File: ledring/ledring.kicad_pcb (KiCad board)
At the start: 2 copper layers, 92 x 92 mm, 22 parts, among them U1 LM3914V, U2 LM3914V

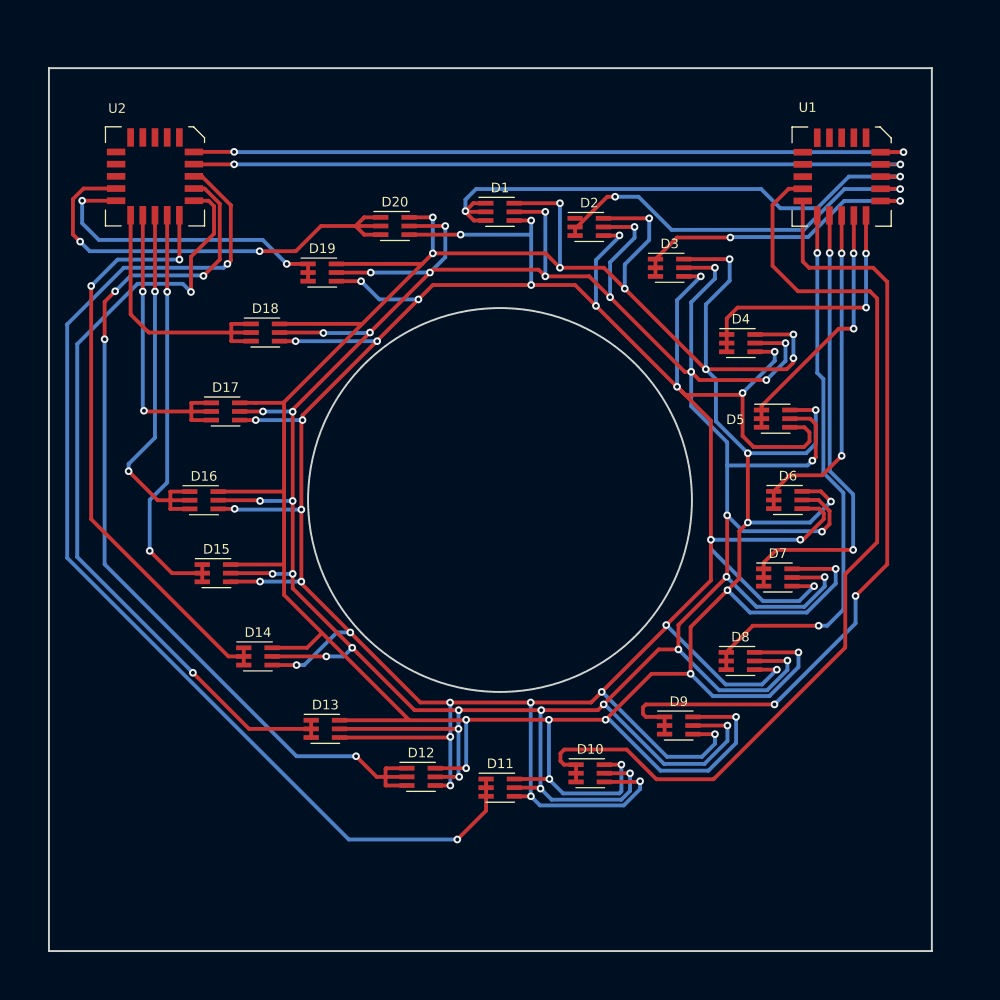
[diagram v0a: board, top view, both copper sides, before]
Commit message: ledring: Adjust PCB routing (angles)
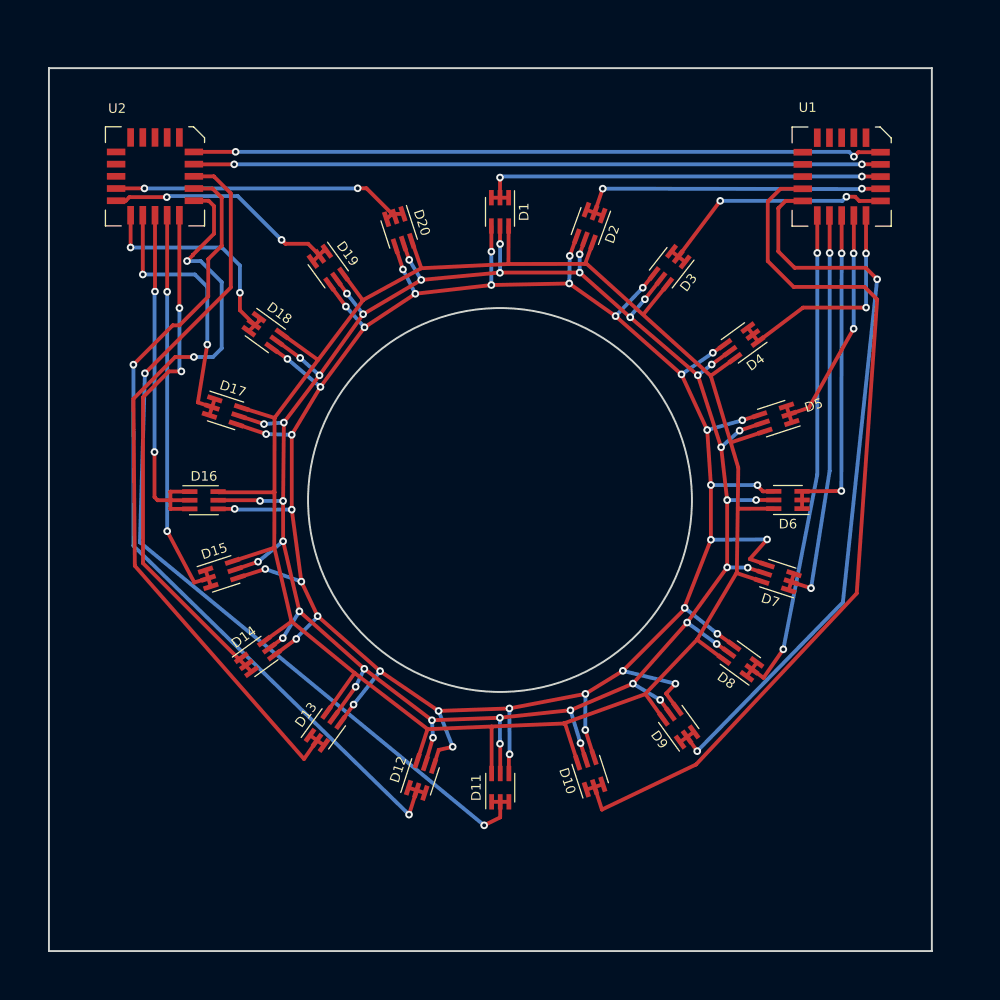
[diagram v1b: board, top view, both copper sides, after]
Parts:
- moved D19 0.80 mm to (112.1, 75.8), turned to -54 degrees
- moved D20 0.61 mm to (119.5, 71.9), turned to -72 degrees
- moved D15 0.56 mm to (101.0, 107.7), turned to 18 degrees
- moved D2 0.11 mm to (139.3, 71.5), turned to -110 degrees
- moved D4 0.06 mm to (155.2, 83.6), turned to -144 degrees
- turned D10 to 108 degrees
- turned D1 to -90 degrees
- turned D11 to 90 degrees
- turned D12 to 72 degrees
- turned D13 to 54 degrees
- turned D14 to 36 degrees
- turned D17 to -18 degrees
- turned D18 to -36 degrees
- turned D3 to -128 degrees
- turned D5 to -162 degrees
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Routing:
- net /BLU: track 394.4 -> 233.4 mm, vias 25 -> 0
- net /GRN: track 397.8 -> 250.4 mm, vias 36 -> 40
- net /RED: track 387.6 -> 274.4 mm, vias 34 -> 40
- net Net-(D11-Pad1): track 115.3 -> 96.4 mm
- net Net-(D20-Pad1): track 47.5 -> 32.2 mm
- net Net-(D1-Pad1): track 58.5 -> 43.6 mm
- net Net-(D12-Pad1): track 97.3 -> 88.3 mm, vias 4 -> 2
- net Net-(D14-Pad1): track 62.9 -> 54.8 mm
- net Net-(D2-Pad1): track 41.2 -> 33.4 mm
- net Net-(D10-Pad1): track 101.4 -> 93.8 mm
- net Net-(D19-Pad1): track 32.0 -> 26.0 mm
- net Net-(D3-Pad1): track 31.9 -> 26.1 mm
- net Net-(D8-Pad1): track 58.0 -> 52.5 mm
- net Net-(D9-Pad1): track 83.6 -> 78.0 mm
- net Net-(D18-Pad1): track 29.5 -> 24.1 mm, vias 0 -> 2
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
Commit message: ledring: switch from LM3914V (PLCC-20) to LM3914N (DIP-18)
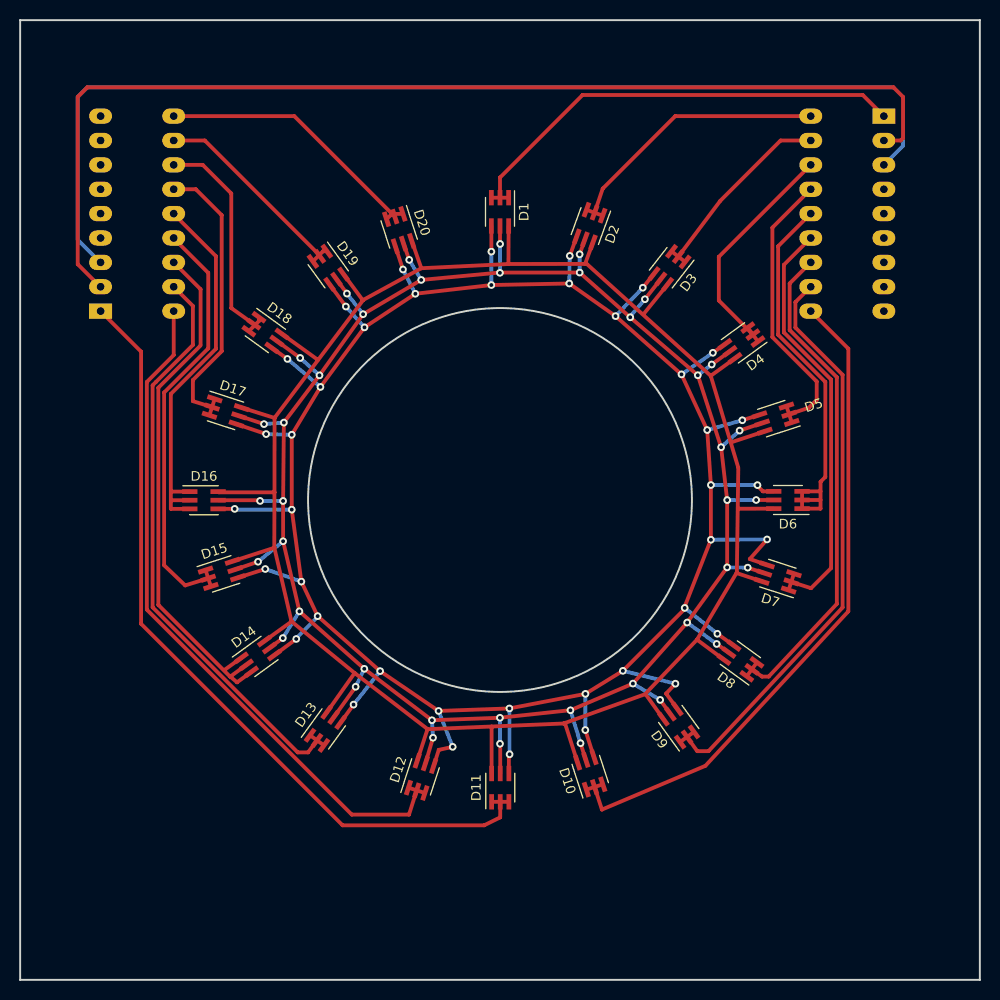
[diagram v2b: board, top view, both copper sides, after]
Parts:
- U1, U2: value LM3914V -> LM3914N; footprint Package_LCC:PLCC-20 -> Package_DIP:DIP-18_W7.62mm_LongPads; moved to B.Cu
- moved U2 15.1 mm to (88.4, 80.3), turned to 0 degrees
- moved U1 7.68 mm to (170.0, 60.0), turned to 180 degrees
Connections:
- U1 pad 10: unconnected-(U1-Pad10) -> Net-(D10-Pad1)
- U1 pad 11: unconnected-(U1-Pad11) -> Net-(D9-Pad1)
- U1 pad 12: Net-(D10-Pad1) -> Net-(D8-Pad1)
- U1 pad 13: Net-(D9-Pad1) -> Net-(D7-Pad1)
- U1 pad 14: Net-(D8-Pad1) -> Net-(D6-Pad1)
- U1 pad 15: Net-(D7-Pad1) -> Net-(D5-Pad1)
- U1 pad 16: Net-(D6-Pad1) -> Net-(D4-Pad1)
- U1 pad 17: Net-(D5-Pad1) -> Net-(D3-Pad1)
- U1 pad 18: Net-(D4-Pad1) -> Net-(D2-Pad1)
- U2 pad 10: unconnected-(U2-Pad10) -> Net-(D20-Pad1)
- U2 pad 11: unconnected-(U2-Pad11) -> Net-(D19-Pad1)
- U2 pad 12: Net-(D20-Pad1) -> Net-(D18-Pad1)
- U2 pad 13: Net-(D19-Pad1) -> Net-(D17-Pad1)
- U2 pad 14: Net-(D18-Pad1) -> Net-(D16-Pad1)
- U2 pad 15: Net-(D17-Pad1) -> Net-(D15-Pad1)
- U2 pad 16: Net-(D16-Pad1) -> Net-(D14-Pad1)
- U2 pad 17: Net-(D15-Pad1) -> Net-(D13-Pad1)
- U2 pad 18: Net-(D14-Pad1) -> Net-(D12-Pad1)
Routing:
- net /V-: track 71.6 -> 113.7 mm, vias 2 -> 0
- net /V+: track 72.0 -> 112.7 mm, vias 2 -> 0
- net Net-(D10-Pad1): track 93.8 -> 70.8 mm
- net Net-(D13-Pad1): track 80.4 -> 61.8 mm, vias 2 -> 0
- net Net-(D9-Pad1): track 78.0 -> 61.4 mm, vias 2 -> 0
- net Net-(D12-Pad1): track 88.3 -> 72.9 mm, vias 2 -> 0
- net Net-(D11-Pad1): track 96.4 -> 84.1 mm, vias 2 -> 0
- net Net-(D6-Pad1): track 34.6 -> 42.0 mm, vias 2 -> 0
- net Net-(D5-Pad1): track 25.2 -> 30.6 mm, vias 2 -> 0
- net Net-(D3-Pad1): track 26.1 -> 21.1 mm, vias 2 -> 0
- net Net-(D1-Pad1): track 43.6 -> 48.4 mm, vias 2 -> 0
- net Net-(D2-Pad1): track 33.4 -> 29.3 mm, vias 2 -> 0
- net Net-(D19-Pad1): track 26.0 -> 22.2 mm, vias 2 -> 0
- net Net-(D20-Pad1): track 32.2 -> 29.3 mm, vias 2 -> 0
- net Net-(D15-Pad1): track 42.3 -> 45.1 mm, vias 2 -> 0
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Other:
- board size 92 x 92 mm -> 100 x 100 mm

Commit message: Exact radial placement of LEDs
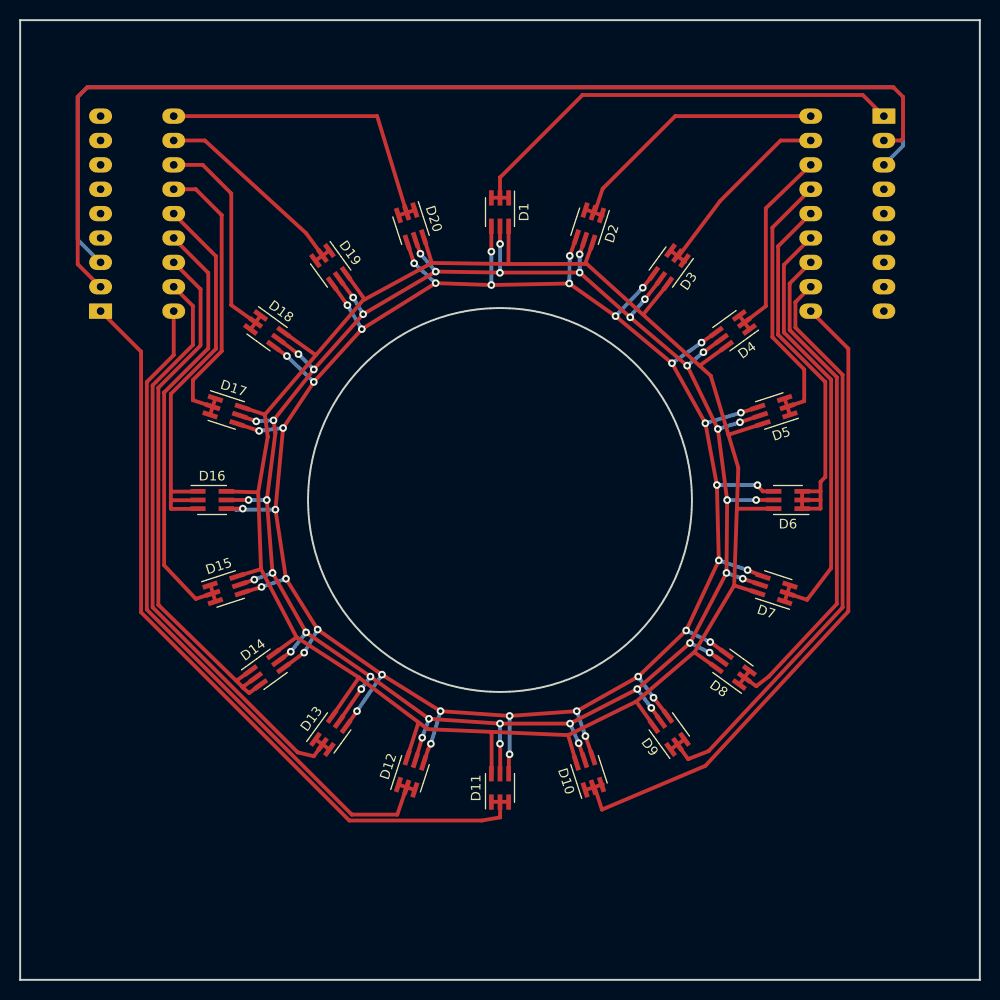
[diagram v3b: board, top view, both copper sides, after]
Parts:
- moved D14 1.64 mm to (105.7, 117.6)
- moved D15 1.64 mm to (101.5, 109.3)
- moved D4 1.55 mm to (154.3, 82.4)
- moved D20 1.30 mm to (120.7, 71.5)
- moved D7 1.27 mm to (158.5, 109.3)
- moved D9 1.26 mm to (147.6, 124.3)
- moved D8 1.16 mm to (154.3, 117.6)
- moved D12 1.09 mm to (120.7, 128.5)
- moved D16 0.85 mm to (100.0, 100.0)
- moved D5 0.82 mm to (158.5, 90.7)
- moved D13 0.71 mm to (112.4, 124.3)
- moved D19 0.28 mm to (112.4, 75.7)
- moved D18 0.26 mm to (105.7, 82.4)
- moved D10 0.13 mm to (139.3, 128.5)
- moved D17 0.08 mm to (101.5, 90.7)
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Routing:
- net /RED: track 274.4 -> 257.2 mm
- net /GRN: track 250.4 -> 240.5 mm
- net /BLU: track 233.4 -> 226.9 mm
- net Net-(D20-Pad1): track 29.3 -> 33.5 mm
- net Net-(D4-Pad1): track 24.9 -> 21.3 mm
- net Net-(D5-Pad1): track 30.6 -> 28.8 mm
- net Net-(D7-Pad1): track 44.5 -> 45.7 mm
- net Net-(D9-Pad1): track 61.4 -> 62.6 mm
- net Net-(D8-Pad1): track 52.7 -> 53.9 mm
- net Net-(D11-Pad1): track 84.1 -> 83.0 mm
- net Net-(D15-Pad1): track 45.1 -> 46.1 mm
- net Net-(D12-Pad1): track 72.9 -> 72.0 mm
- net Net-(D13-Pad1): track 61.8 -> 62.4 mm
- net Net-(D14-Pad1): track 56.2 -> 56.8 mm

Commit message: ledring: update routing
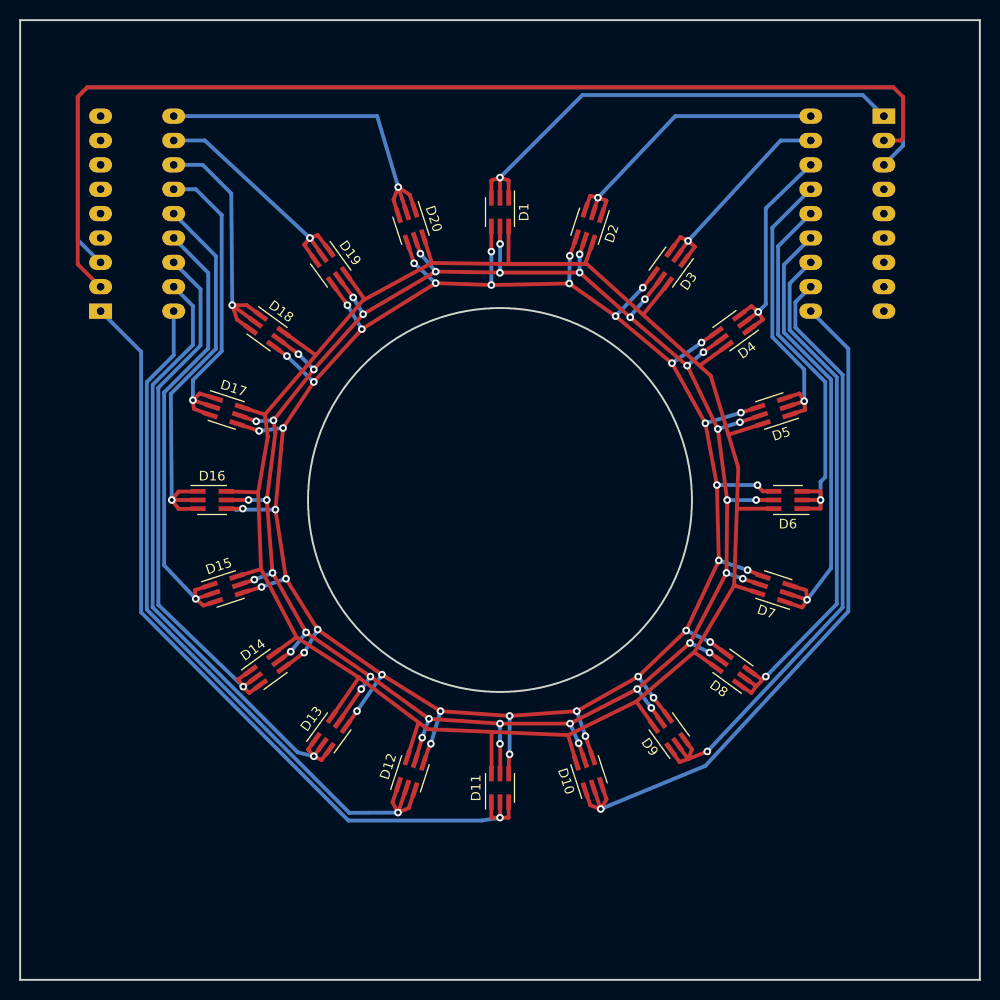
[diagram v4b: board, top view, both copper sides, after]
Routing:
- net Net-(D18-Pad1): track 23.8 -> 28.5 mm, vias 0 -> 1
- net Net-(D20-Pad1): track 33.5 -> 38.0 mm, vias 0 -> 1
- net Net-(D12-Pad1): track 72.0 -> 76.4 mm, vias 0 -> 1
- net Net-(D19-Pad1): track 22.3 -> 26.3 mm, vias 0 -> 1
- net Net-(D7-Pad1): track 45.7 -> 49.6 mm, vias 0 -> 1
- net Net-(D10-Pad1): track 70.8 -> 74.7 mm, vias 0 -> 1
- net Net-(D1-Pad1): track 48.4 -> 52.1 mm, vias 0 -> 1
- net Net-(D17-Pad1): track 30.6 -> 34.2 mm, vias 0 -> 1
- net Net-(D3-Pad1): track 21.1 -> 24.6 mm, vias 0 -> 1
- net Net-(D5-Pad1): track 28.8 -> 32.1 mm, vias 0 -> 1
- net Net-(D4-Pad1): track 21.3 -> 24.7 mm, vias 0 -> 1
- net Net-(D11-Pad1): track 83.0 -> 86.3 mm, vias 0 -> 1
- net Net-(D2-Pad1): track 29.3 -> 32.4 mm, vias 0 -> 1
- net Net-(D9-Pad1): track 62.6 -> 65.7 mm, vias 0 -> 1
- net Net-(D15-Pad1): track 46.1 -> 49.1 mm, vias 0 -> 1
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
